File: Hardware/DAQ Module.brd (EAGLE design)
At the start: 70 x 70 mm, 32 parts, among them IC2 LM4040AIM3-2.0_NOPB, J1 393570014, J2 MF-CON-2.54mm-01x06, J3 393570014, J4 MF-CON-2.54mm-01x06, J5 MF-CON-2.54mm-01x06, J6 UJ2-MIBH2-4-SMT-TR, SW1 SPST_TACT-KMR2, U1 ATMEGA32U4TQFP, Y1 16MHz

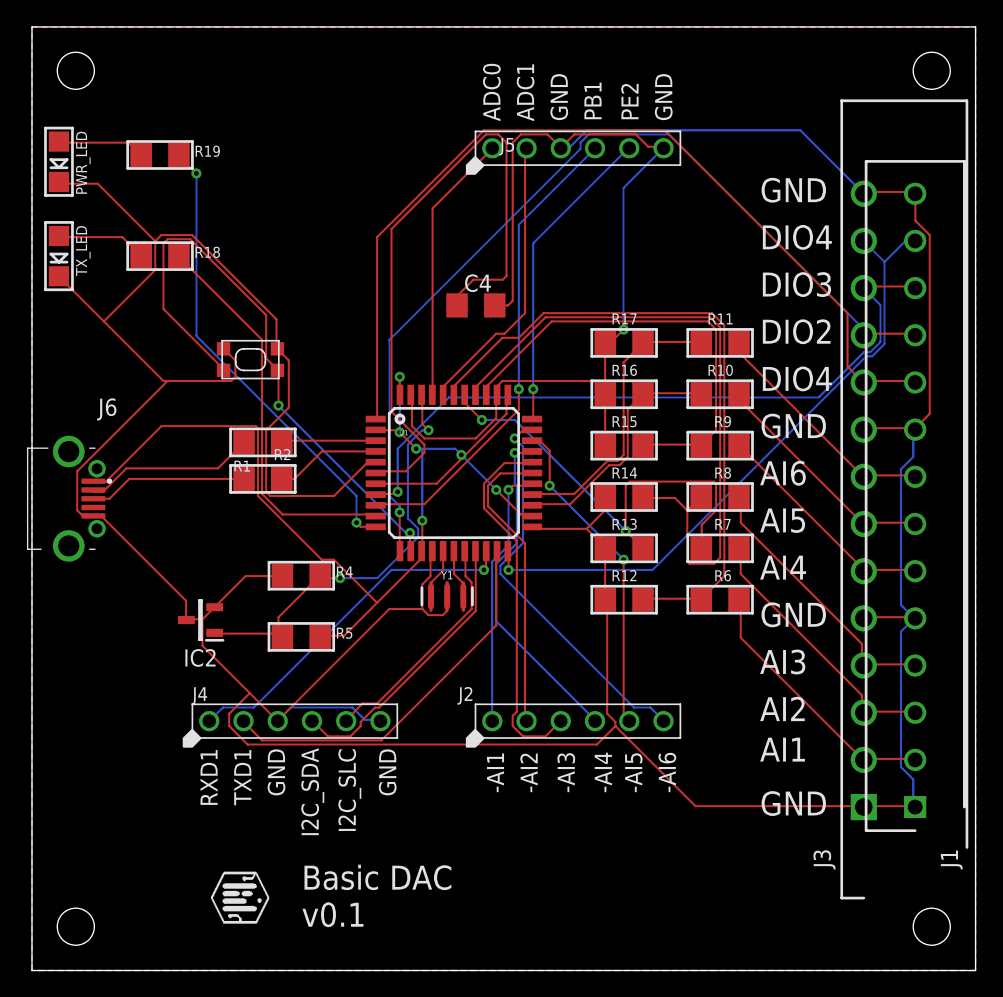
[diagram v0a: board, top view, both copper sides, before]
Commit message: Hardware updates.
- Remapping of ports for easier prototyping.
- Addition of serial programming port.
- New smaller board layout.
- Higher analog imput impedance.
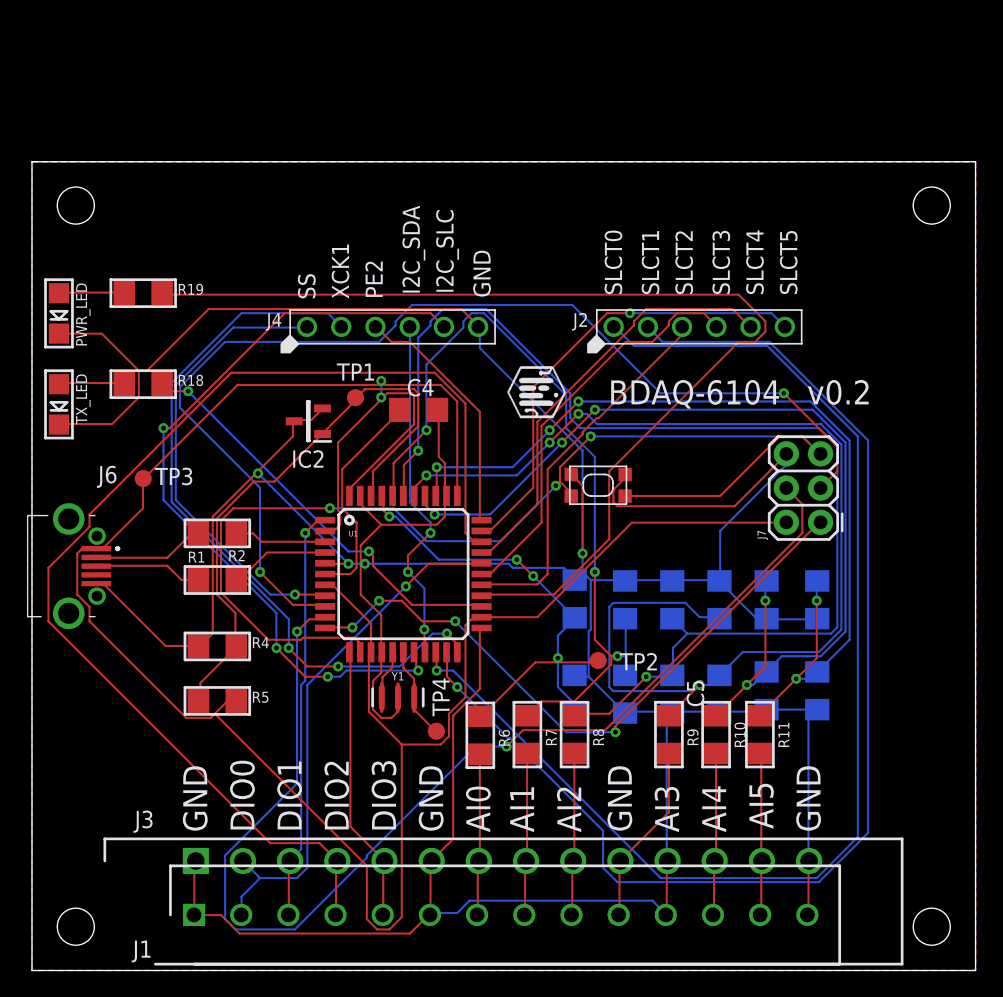
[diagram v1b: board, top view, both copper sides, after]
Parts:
- removed J5: MF-CON-2.54mm-01x06, MF_Connectors:PTH_2.54MM_01X06
- added C1, C2, C3, C5, C6, C7: 220pF, adafruit:C1206
- added J7: SPP, SparkFun-Connectors:2X3
- added TP1, TP2, TP3, TP4: TPB1,27, testpad:B1,27
- R10, R11, R6, R7, R8, R9: value 20k -> 1M
- R12, R13, R14, R15, R16, R17: value 5k -> 255K
- moved J1 54.1 mm to (12.0, 4.12), turned to 0 degrees
- moved J3 49.7 mm to (12.2, 8.12), turned to 0 degrees
- moved U$1 43.5 mm to (35.2, 41.0)
- moved J2 30.6 mm to (49.5, 47.8)
- moved J4 30.1 mm to (26.8, 47.8)
- moved R11 29.2 mm to (54.0, 17.5), turned to 270 degrees
- moved SW1 27.4 mm to (42.0, 36.0)
- moved R10 25.3 mm to (50.8, 17.5), turned to 270 degrees
- moved R17 23.8 mm to (58.2, 27.5), flipped to the bottom, turned to 90 degrees
- moved R9 21.8 mm to (47.2, 17.5), turned to 270 degrees
- moved R8 20.7 mm to (40.2, 17.5), turned to 270 degrees
- moved R6 20.4 mm to (33.3, 17.4), turned to 270 degrees
- moved R7 19.9 mm to (36.8, 17.5), turned to 270 degrees
- moved R16 18.6 mm to (54.5, 27.5), flipped to the bottom, turned to 90 degrees
- moved IC2 16.8 mm to (20.5, 40.8)
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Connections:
- net -AI6 renamed SLCT5
- net N$4 renamed XTAL2
- removed net -AI1: J2.P$1, U1.27
- removed net -AI2: J2.P$2, U1.28
- removed net -AI3: J2.P$3, U1.29
- removed net -AI4: J2.P$4, U1.30
- removed net -AI5: J2.P$5, U1.31
- removed net ADC0: J5.P$1, U1.41
- removed net ADC1: J5.P$2, U1.40
- removed net AI6: R11.1, R17.2, U1.26
- removed net AI6_IN: J1.8, J3.8, R11.2
- removed net DIO4: J1.13, J3.13, U1.22
- removed net N$3: U1.17, Y1.3
- removed net PB1: J5.P$4, U1.9
- removed net RXD1: J4.P$1, U1.20
- removed net TXD1: J4.P$2, U1.21
- new net AI0: C1.1, R12.2, R6.1, TP2.TP, U1.41
- new net AI0_IN: J1.7, J3.7, R6.2
- new net DIO0: J1.2, J3.2, U1.29
- new net MISO: J7.1, U1.11
- new net MOSI: J7.4, U1.10
- new net SCK: J7.3, U1.9
- new net SLCT0: J2.P$1, U1.20
- new net SLCT1: J2.P$2, U1.21
- new net SLCT2: J2.P$3, U1.27
- new net SLCT3: J2.P$4, U1.28
- new net SLCT4: J2.P$5, U1.30
- new net SS: J4.P$1, U1.8
- new net XCK1: J4.P$2, U1.22
- new net XTAL1: TP4.TP, U1.17, Y1.3
- net AI1: now also C2.1, R13.2, R7.1, U1.40; no longer R12.2, R6.1, U1.39
- net AI1_IN: now also J1.8, J3.8, R7.2; no longer J1.2, J3.2, R6.2
- net AI2: now also C3.1, R14.2, R8.1, U1.39; no longer R13.2, R7.1, U1.38
- net AI2_IN: now also J1.9, J3.9, R8.2; no longer J1.3, J3.3, R7.2
- net AI3: now also C5.1, R15.2, R9.1, U1.38; no longer R14.2, R8.1, U1.37
- net AI3_IN: now also J1.10, J3.10, R9.2; no longer J1.4, J3.4, R8.2
- net AI4: now also C6.1, R10.1, R16.2, U1.37; no longer R15.2, R9.1, U1.36
- net AI4_IN: now also J1.12, J3.12, R10.2; no longer J1.6, J3.6, R9.2
- net AI5: now also C7.1, R11.1, R17.2, U1.36; no longer R10.1, R16.2, U1.25
- net AI5_IN: now also J1.13, J3.13, R11.2; no longer J1.7, J3.7, R10.2
- net AREF: now also TP1.TP
- net DIO1: now also J1.3, J3.3; no longer J1.10, J3.10
- net DIO2: now also J1.4, J3.4, U1.31; no longer J1.11, J3.11, U1.12
- net DIO3: now also J1.5, J3.5, U1.12; no longer J1.12, J3.12, U1.8
- net GND: now also C1.2, C2.2, C3.2, C5.2, C6.2, C7.2, J1.11, J1.6, J3.11, J3.6, J7.6; no longer J1.5, J1.9, J3.5, J3.9, J4.P$3, J5.P$3, J5.P$6
- net PE2: now also J4.P$3; no longer J5.P$5
- net PWR_LED: now also U1.26; no longer U1.11
- net RESET: now also J7.5
- net TX_LED: now also U1.25; no longer U1.10
- net V_USB: now also J7.2, TP3.TP
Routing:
- net V_USB: track 82.5 -> 177.9 mm, vias 6 -> 2
- net SLCT0: track 0.00 -> 91.4 mm, vias 0 -> 1
- net SLCT1: track 0.00 -> 91.4 mm, vias 0 -> 1
- net MOSI: track 0.00 -> 85.3 mm, vias 0 -> 2
- net SCK: track 0.00 -> 81.5 mm, vias 0 -> 2
- net AI2: track 33.8 -> 88.0 mm
- net XCK1: track 0.00 -> 53.4 mm, vias 0 -> 3
- net AI5: track 18.1 -> 67.7 mm, vias 0 -> 5
- net MISO: track 0.00 -> 48.3 mm, vias 0 -> 4
- net DIO4: track 47.4 -> 0.00 mm, vias 1 -> 0
- net PWR_LED: track 34.3 -> 78.5 mm, vias 2 -> 0
- net RESET: track 43.5 -> 86.6 mm, vias 2 -> 3
- net GND: track 379.4 -> 338.0 mm, vias 1 -> 4
- net I2C_SLC: track 17.3 -> 57.6 mm, vias 0 -> 4
- net DIO0: track 0.00 -> 39.1 mm, vias 0 -> 1
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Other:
- board size 70 x 70 mm -> 70 x 60 mm
- board text added: "AI0"
- board text added: "BDAQ-6104"
- board text added: "DIO0"
- board text added: "DIO1"
- board text added: "SLCT0"
- board text added: "SLCT1"
- board text added: "SLCT2"
- board text added: "SLCT3"
- board text added: "SLCT4"
- board text added: "SLCT5"
- board text added: "SS"
- board text added: "XCK1"
- board text added: "v0.2"
- board text removed: "-AI1"
- board text removed: "-AI2"
- board text removed: "-AI3"
- board text removed: "-AI4"
- board text removed: "-AI5"
- board text removed: "-AI6"
- board text removed: "ADC0"
- board text removed: "ADC1"
- board text removed: "AI6"
- board text removed: "Basic DAC"
- board text removed: "DIO4"
- board text removed: "PB1"
- board text removed: "RXD1"
- board text removed: "TXD1"
- board text removed: "v0.1"

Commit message: Hardware updates and corresponding SW updates.
- Updated analog input circuitry to use a 4.096 ARef.
- Added analog input filtering.
- Updated firmware to utilize new analog input circuitry.
- Some general clean up of firmware.
- Updated examples in LabView driver.
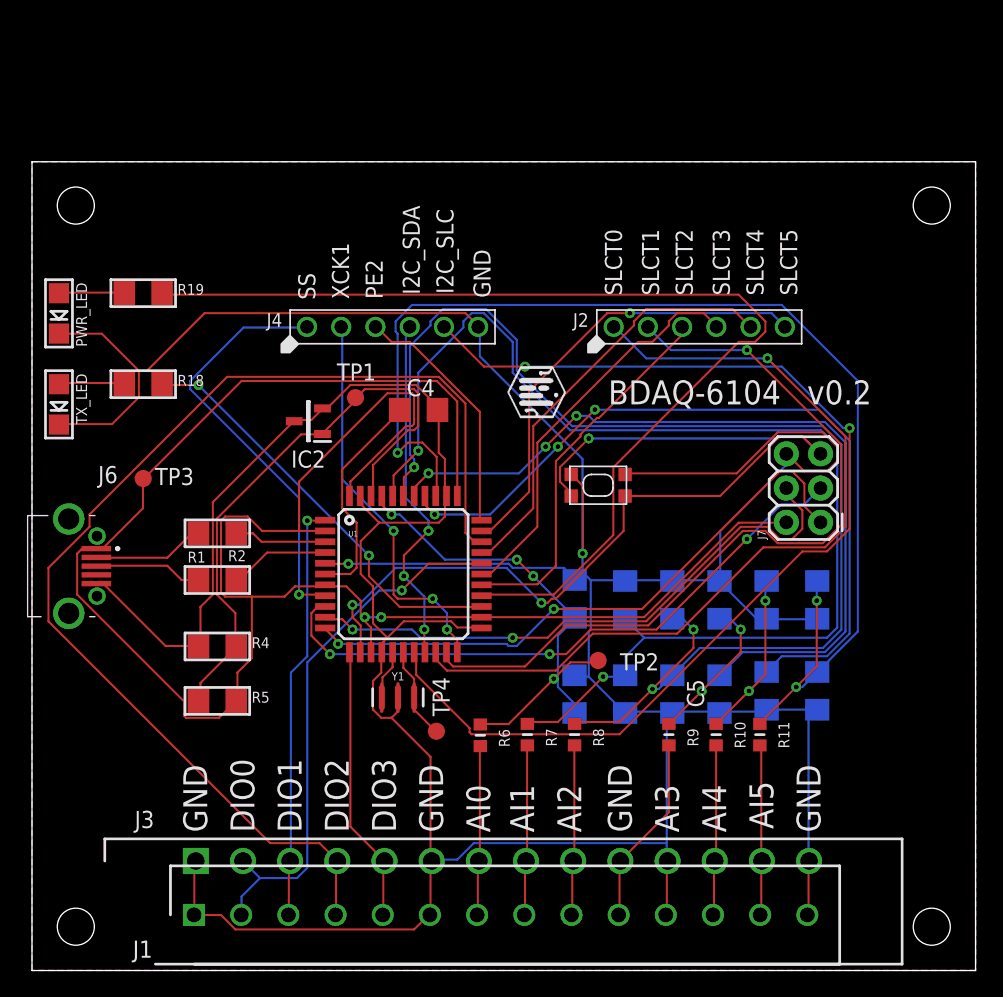
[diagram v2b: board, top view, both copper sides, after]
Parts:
- C1, C2, C3, C5, C6, C7: value 220pF -> 470pF
- IC2: value LM4040AIM3-2.0_NOPB -> LM4040AIM3-4.1_NOPB; device LM4040AIM3-2.0_NOPB:SOT95P237X95-3N -> LM4040AIM3-4.1_NOPB:SOT95P237X112-3N
- R10, R11, R6, R7, R8, R9: value 1M -> 590K; device microbuilder:1206 -> ERJ3RED5903V:RESC1608X55N
- R12, R13, R14, R15, R16, R17: value 255K -> 402K
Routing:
- net MOSI: track 85.3 -> 43.7 mm
- net SCK: track 81.5 -> 46.3 mm, vias 2 -> 3
- net SLCT1: track 91.4 -> 59.1 mm
- net AI1: track 60.0 -> 90.7 mm, vias 3 -> 2
- net SLCT0: track 91.4 -> 62.9 mm
- net I2C_SLC: track 57.6 -> 82.9 mm, vias 4 -> 2
- net XCK1: track 53.4 -> 29.2 mm
- net AI5: track 67.7 -> 90.7 mm, vias 5 -> 3
- net V_USB: track 177.9 -> 158.6 mm
- net RESET: track 86.6 -> 71.1 mm
- net AI3: track 86.4 -> 73.3 mm, vias 4 -> 5
- net GND: track 338.0 -> 344.5 mm, vias 4 -> 2
- net AI2: track 88.0 -> 94.4 mm, vias 2 -> 3
- net MISO: track 48.3 -> 45.3 mm, vias 4 -> 2
- net SS: track 34.1 -> 31.5 mm
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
